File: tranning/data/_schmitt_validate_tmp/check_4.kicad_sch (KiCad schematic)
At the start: 3 parts, among them U1 LM358

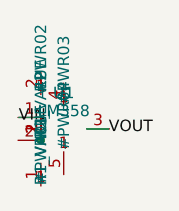
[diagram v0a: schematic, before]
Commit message: Fix overlapping and mis-wired schematics; add ESP32, Mega 2560, Pi 5
- circuit_rule_check.transform_point: flip the library y axis. Verified
  against KiCad's own demo schematics (42/42 and 182/182 pins on a wire);
  the old formula made generated files open in KiCad with +5V on the GND
  pin and the reset pull-up on PB0.
- circuit_ic_generator: rewritten layout. IC pins get a short stub to an
  outward-facing power symbol or a net label; decoupling, reset and
  crystal circuits are measured blocks stacked beside the IC, checked for
  overlap before writing; drawing placed on an auto-sized page; library
  symbols get graphics. Adds ESP32-WROOM-32, ATmega2560, Pi 5 header.
- circuit_rule_check: same-name nets are joined (KiCad behaviour), new
  overlapping_symbols rule, 3V3/EN pin names recognised.
- circuit_kicad_to_schemdraw: draws labels, power flags and IC pin names;
  pin side taken from the pin's own direction.
- schmitt_trigger_gen: library block fixed so KiCad wires IN+/IN- and
  V+/V- as intended and power pins join GND/VCC; model output unchanged.
- Tests: 65 pass, including a real kicad-cli netlist check.

Co-Authored-By: Claude Opus 5.5 <noreply@anthropic.com>
Claude-Session: https://claude.ai/code/session_01TWSKnHncRvWd1K9A45SkP5
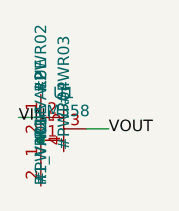
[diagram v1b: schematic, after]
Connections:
- net VIN: now also U1.2; no longer U1.1
- net at R1.1: now also R2.2, U1.1
- net VCC: now reaches U1.4
- net VCC: now also R1.2
- net GND: now reaches U1.5
- net GND: now also R2.1
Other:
- moved on the sheet: R1, R2, U1

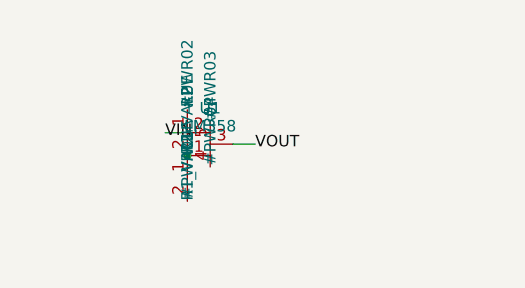
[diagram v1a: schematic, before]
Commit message: Redesign Schmitt-trigger templates without overlaps (retrain in progress)
- schmitt_trigger_gen: KiCad-sized op-amp/resistor/inverter symbols with
  graphics; every pin position computed with transform_point; orthogonal
  wiring with the feedback resistor routed above/below the op-amp; labels
  and power-net names placed away from parts; power references hidden.
  uuids are added by wrap_kicad() instead of the model (~90 tokens less
  per circuit), so the longest pair is 990 tokens (block_size 1024).
  validate_pairs now rejects overlap warnings too.
- circuit_rule_check: a multi-pin part's body is where its pins end (tip
  plus pin length), so supply symbols on an op-amp's V+/V- tips are not
  counted as overlapping it.
- schmitt_trigger_train: --checkpoint-every (default 10) for long runs.
- Tests: real-KiCad netlist check for four topologies; context-length check.

The checked-in schmitt model still matches the old templates until the
retrain running now finishes.

Co-Authored-By: Claude Opus 5.5 <noreply@anthropic.com>
Claude-Session: https://claude.ai/code/session_01TWSKnHncRvWd1K9A45SkP5
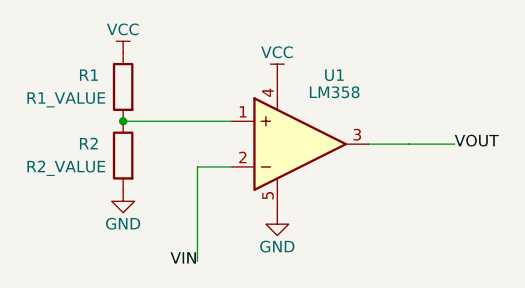
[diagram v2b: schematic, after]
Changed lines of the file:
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@@
 (kicad_sch (version 20231120) (generator sinco_schmitt_gen) (paper "A4")
- (symbol (lib_id "Sinco:R") (at 107.46 103.81 90) (unit 1)(property "Reference" "R1" (at 107.46 99.81 0)) (property "Value" "R1_VALUE" (at 107.46 101.81 0)))(symbol (lib_id "Sinco:R") (at 107.46 98.72999999999999 90) (unit 1)(property "Reference" "R2" (at 107.46 94.72999999999999 0)) (property "Value" "R2_VALUE" (at 107.46 96.72999999999999 0)))(symbol (lib_id "Sinco:OpAmp") (at 110.0 100.0 0) (unit 1)(property "Reference" "U1" (at 110.0 96.0 0)) (property "Value" "LM358" (at 110.0 98.0 0)))(symbol (lib_id "power:VCC") (at 107.46 106.35000000000001 90) (unit 1)(property "Reference" "#PWR01" (at 107.46 102.35000000000001 0)) )(symbol (lib_id "power:GND") (at 107.46 96.18999999999998 90) (unit 1)(property "Reference" "#PWR02" (at 107.46 92.18999999999998 0)) )(symbol (lib_id "power:GND") (at 110.0 97.46 90) (unit 1)(property "Reference" "#PWR03" (at 110.0 93.46 0)) )(symbol (lib_id "power:VCC") (at 110.0 102.54 90) (unit 1)(property "Reference" "#PWR04" (at 110.0 98.54 0)) )(wire (pts (xy 105.0 98.73) (xy 107.46 98.73)))(wire (pts (xy 112.54 100.0) (xy 115.0 100.0)))(junction (at 107.46 101.27))(label "VIN" (at 105.0 98.73 0))(label "VOUT" (at 115.0 100.0 0)))
+ (symbol (lib_id "Sinco:R") (at 100.33 93.64999999999999 90) (unit 1) (property "Reference" "R1" (at 96.52 92.38 90)) (property "Value" "R1_VALUE" (at 93.98 94.91999999999999 90)))(symbol (lib_id "Sinco:R") (at 100.33 101.27 90) (unit 1) (property "Reference" "R2" (at 96.52 100.0 90)) (property "Value" "R2_VALUE" (at 93.98 102.53999999999999 90)))(symbol (lib_id "Sinco:OpAmp") (at 120.0 100.0 0) (unit 1) (property "Reference" "U1" (at 123.81 92.38 0)) (property "Value" "LM358" (at 123.81 94.285 0)))(symbol (lib_id "power:VCC") (at 117.46 92.38 0) (unit 1) (property "Reference" "#PWR01" (at 117.46 88.316 0) (effects hide)) (property "Value" "VCC" (at 117.46 89.83999999999999 0)))(symbol (lib_id "power:GND") (at 117.46 107.62 0) (unit 1) (property "Reference" "#PWR02" (at 117.46 103.55600000000001 0) (effects hide)) (property "Value" "GND" (at 117.46 111.43 0)))(wire (pts (xy 127.62 100.0) (xy 132.08 100.0)))(wire (pts (xy 132.08 100.0) (xy 137.16 100.0)))(symbol (lib_id "power:VCC") (at 100.33 89.84 0) (unit 1) (property "Reference" "#PWR03" (at 100.33 85.77600000000001 0) (effects hide)) (property "Value" "VCC" (at 100.33 87.3 0)))(symbol (lib_id "power:GND") (at 100.33 105.08 0) (unit 1) (property "Reference" "#PWR04" (at 100.33 101.01599999999999 0) (effects hide)) (property "Value" "GND" (at 100.33 108.89 0)))(wire (pts (xy 100.33 97.46) (xy 112.38 97.46)))(wire (pts (xy 108.585 113.03) (xy 108.585 102.54)))(wire (pts (xy 108.585 102.54) (xy 112.38 102.54)))(junction (at 100.33 97.46))(label "VIN" (at 108.585 113.03 180))(label "VOUT" (at 137.16 100.0 0)))
